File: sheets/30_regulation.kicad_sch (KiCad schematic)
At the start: 0 parts

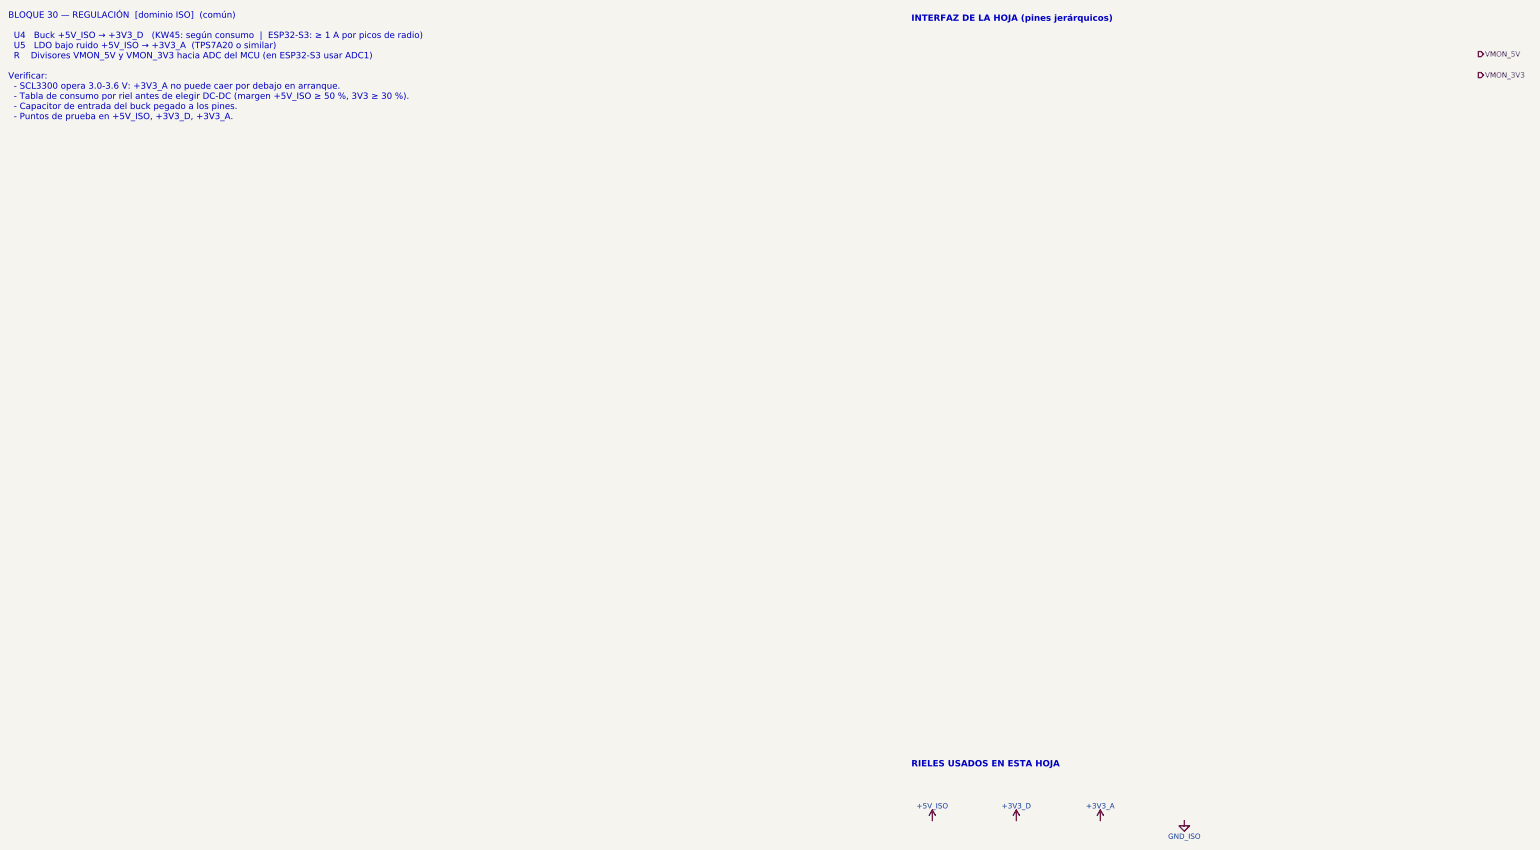
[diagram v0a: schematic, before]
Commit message: 30_regulation: buck TPS62A02-Q1 (+3V3_D), LDO LP5907-Q1 (+3V3_A) y VMON
- U301 TPS62A02QDRLRQ1 (+5V_ISO -> +3V3_D, 2 A, 2.2 MHz, PSM):
  L301 XAL4020-102MEC 1 uH (Isat 8.7 A); FB R303 453k / R304 100k ->
  3.318 V, C_FF C303 10 pF (TI); C_IN 10 uF 0805 + 100 nF; C_OUT C304
  22 uF 0805 (presupuesto de 47 uF en +3V3_D con el módulo); EN con
  pull-up; PG con pull-up a +3V3_D y test point.
- U302 LP5907QMFX-3.3Q1 (+5V_ISO -> +3V3_A) detrás de la ferrita FB301,
  C_IN/C_OUT 1 uF, PWR_FLAG en la entrada.
- VMON_5V (100k/49.9k) y VMON_3V3 (100k/100k) con 100 nF hacia ADC1.
- Test points en +5V_ISO, +3V3_D, +3V3_A, GND_ISO y PG.
- Símbolos TPS62A02QDRLRQ1 y TPS7A1650QDGNRQ1 (easyeda2kicad) reescritos:
  tipos de pin según TI, fabricante y datasheet de TI, y huellas
  oficiales de KiCad (SOT-563 y HVSSOP-8 EP1.57x1.89 con vías), que se
  acercan más a los land patterns TI DRL0006A y DGN0008B/C que las de
  EasyEDA. Huellas EasyEDA con ruta 3D ${KIPRJMOD}.

ERC de la hoja: 0 violaciones (total del proyecto 160 -> 149).
sch_visual_qa: PASS.

Co-Authored-By: Claude Opus 5.5 <noreply@anthropic.com>
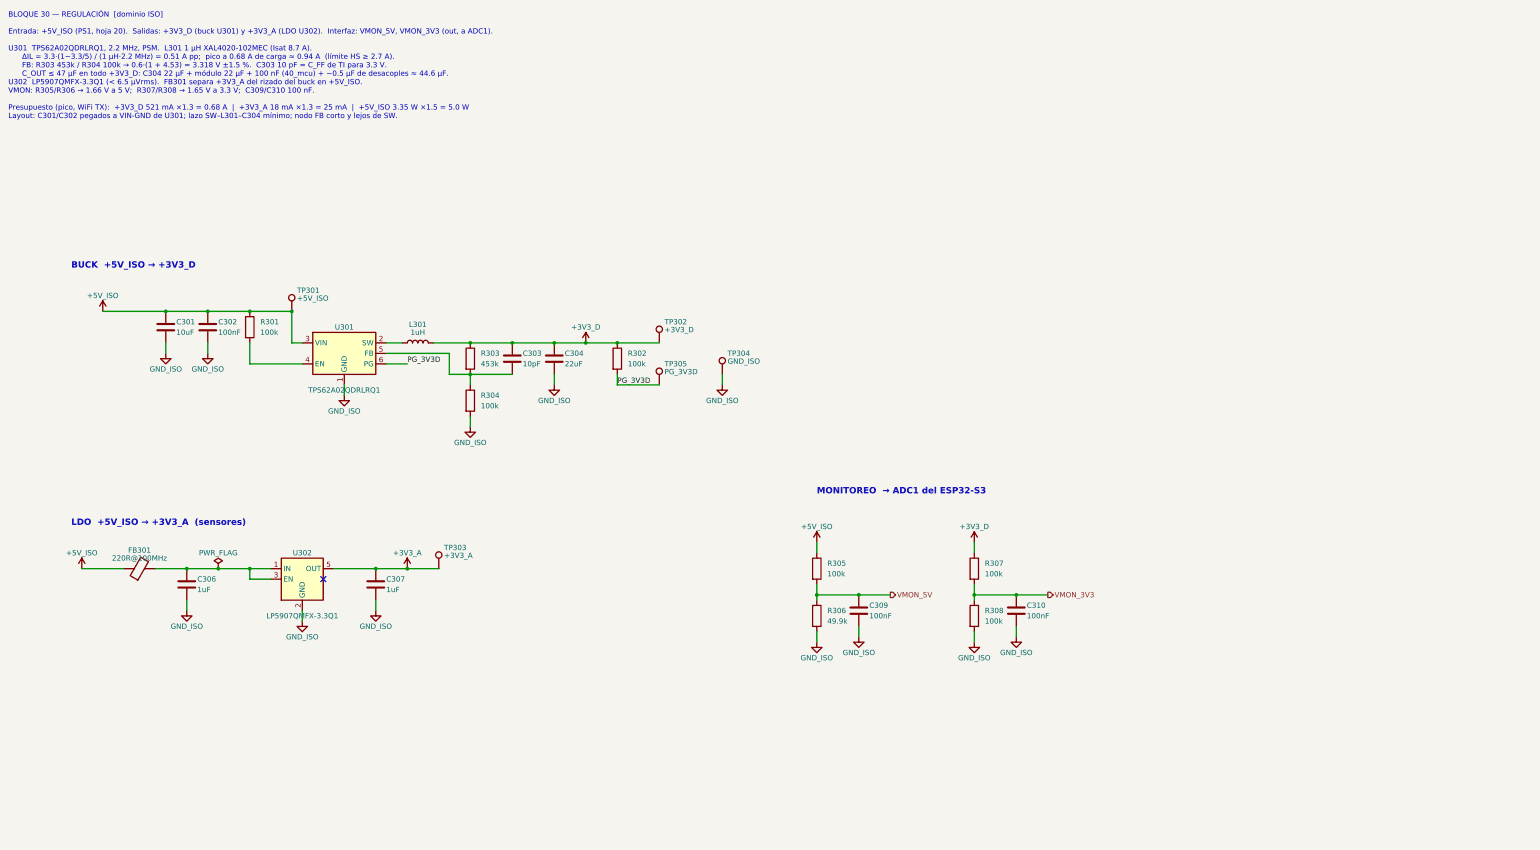
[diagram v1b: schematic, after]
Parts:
- added C301: 10uF, Capacitor_SMD:C_0805_2012Metric, symbol Device:C
- added C302, C309, C310: 100nF, Capacitor_SMD:C_0603_1608Metric, symbol Device:C
- added C303: 10pF, Capacitor_SMD:C_0603_1608Metric, symbol Device:C
- added C304: 22uF, Capacitor_SMD:C_0805_2012Metric, symbol Device:C
- added C306, C307: 1uF, Capacitor_SMD:C_0603_1608Metric, symbol Device:C
- added FB301: 220R@100MHz, Inductor_SMD:L_0603_1608Metric, symbol Device:FerriteBead
- added L301: 1uH, Inductor_SMD:L_Coilcraft_XAL4020-XXX, symbol Device:L
- added R301, R302, R304, R305, R307, R308: 100k, Resistor_SMD:R_0603_1608Metric, symbol Device:R
- added R303: 453k, Resistor_SMD:R_0603_1608Metric, symbol Device:R
- added R306: 49.9k, Resistor_SMD:R_0603_1608Metric, symbol Device:R
- added TP301: +5V_ISO, TestPoint:TestPoint_Pad_D1.5mm, symbol Connector:TestPoint
- added TP302: +3V3_D, TestPoint:TestPoint_Pad_D1.5mm, symbol Connector:TestPoint
- added TP303: +3V3_A, TestPoint:TestPoint_Pad_D1.5mm, symbol Connector:TestPoint
- added TP304: GND_ISO, TestPoint:TestPoint_Pad_D1.5mm, symbol Connector:TestPoint
- added TP305: PG_3V3D, TestPoint:TestPoint_Pad_D1.5mm, symbol Connector:TestPoint
- added U301: TPS62A02QDRLRQ1, Package_TO_SOT_SMD:SOT-563, symbol easyeda2kicad:TPS62A02QDRLRQ1
- added U302: LP5907QMFX-3.3Q1, Package_TO_SOT_SMD:SOT-23-5, symbol Regulator_Linear:LP5907MFX-3.3
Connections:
- net +3V3_A: now also C307.1, TP303.1, U302.5 (OUT)
- net +3V3_D: now also C303.1, C304.1, L301.2, R302.1, R303.1, R307.1, TP302.1
- net +5V_ISO: now also C301.1, C302.1, FB301.1, R301.1, R305.1, TP301.1, U301.3 (VIN)
- net GND_ISO: now also C301.2, C302.2, C304.2, C306.2, C307.2, C309.2, C310.2, R304.2, R306.2, R308.2, TP304.1, U301.1 (GND), U302.2 (GND)
- net VMON_3V3: now also C310.1, R307.2, R308.1
- net VMON_5V: now also C309.1, R305.2, R306.1
- new net: C303.2, R303.2, R304.1, U301.5 (FB)
- new net: C306.1, FB301.2, U302.1 (IN), U302.3 (EN)
- new net: L301.1, U301.2 (SW)
- new net: R301.2, U301.4 (EN)
- new net PG_3V3D: R302.2, TP305.1, U301.6 (PG)
- no-connect marks 0 -> 1
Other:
- note added: "BLOQUE 30 — REGULACIÓN [dominio ISO] Entrada: +5V_ISO (PS1, hoja 20). Salidas: +3V3_D (buck U301) y +3V3_A (LDO U302). Interfaz: VMON_5V, VMON_3V3 (out, a ADC1). U301 TPS62A02QDRLRQ1, 2.2 MHz, PSM. L301 1 µH XAL4020-102MEC (Isat 8.7 A). ΔIL = 3.3·(1−3.3/5) / (1 µH·2.2 MHz) = 0.51 A pp; pico a 0.68 A de carga ≈ 0.94 A (límite HS ≥ 2.7 A). FB: R303 453k / R304 100k → 0.6·(1 + 4.53) = 3.318 V ±1.5 %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"
- note added: "BUCK +5V_ISO → +3V3_D"
- note added: "LDO +5V_ISO → +3V3_A (sensores)"
- note added: "MONITOREO → ADC1 del ESP32-S3"
- note removed: "BLOQUE 30 — REGULACIÓN [dominio ISO] (común) U4 Buck +5V_ISO → +3V3_D (KW45: según consumo | ESP32-S3: ≥ 1 A por picos de radio) U5 LDO bajo ruido +5V_ISO → +3V3_A (TPS7A20 o similar) R Divisores VMON_5V y VMON_3V3 hacia ADC del MCU (en ESP32-S3 usar ADC1) Verificar: - SCL3300 opera 3.0-3.6 V: +3V3_A no puede caer por debajo en arranque. - Tabla de consumo por riel antes de elegir DC-DC (margen +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"
- note removed: "INTERFAZ DE LA HOJA (pines jerárquicos)"
- note removed: "RIELES USADOS EN ESTA HOJA"

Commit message: 20_isolation: PS201 EC4AW8-48S05, LDO +5V_VEH, ISO7763-Q1; PWR_FLT_N; L301 HandSolder
- Hoja 20 completa: PS201 Cincon EC4AW8-48S05 (sin Remote On/Off) con
  C201/C202/C203; U201 TPS7A1650-Q1 (+VPROT -> +5V_VEH; DELAY, PG y FB/NC
  abiertos según TI SBVS188E tabla 5-1); U202 ISO7763FQDWRQ1 con pull-downs
  R201-R204; notas de distancias de la barrera 1.
- Símbolo INCLI-VA:EC4AW8-48S05 creado desde la tabla de pines del datasheet
  Cincon V10 (excepción autorizada); huella oficial TRACO THD 15WIN verificada.
- Renombre PWR_FLT -> PWR_FLT_N en la raíz, 20 y 40_mcu.
- Huella INCLI-VA:L_Coilcraft_XAL4020_HandSolder (Coilcraft Doc 806-4,
  rev. 02/25/26) asignada a L301.
- Datasheets de EC4AW8 y XAL4020 en docs/datasheets.
- ERC: 0 en 20 y 30 (129 en el proyecto); sch_visual_qa PASS en 20.

Co-Authored-By: Claude Opus 5.5 <noreply@anthropic.com>
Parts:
- L301: footprint Inductor_SMD:L_Coilcraft_XAL4020-XXX -> INCLI-VA:L_Coilcraft_XAL4020_HandSolder; Notes 1.0 uH +-20 %, Isat 8.7 A, DCR 14.6 mohm máx, AEC-Q200. Isat > límite de corriente de U301 (3.3 A máx) para soportar el corto. TI admite 0.3-1.2 uH efectivos. Huella oficial KiCad. -> 1.0 uH +-20 %, Isat 8.7 A, DCR 14.6 mohm máx, AEC-Q200. Isat > límite de corriente de U301 (3.3 A máx) para soportar el corto. TI admite 0.3-1.2 uH efectivos. Huella INCLI-VA:L_Coilcraft_XAL4020_HandSolder: land pattern de Coilcraft Doc 806-4 (rev. 02/25/26, 0.98 x 3.4 mm, centros 2.37 mm) con pads extendidos 1 mm fuera del cuerpo para soldar a mano. En producción volver a Inductor_SMD:L_Coilcraft_XAL4020-XXX.
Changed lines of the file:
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@@
 			)
 		)
-		(property "Footprint" "Inductor_SMD:L_Coilcraft_XAL4020-XXX"
+		(property "Footprint" "INCLI-VA:L_Coilcraft_XAL4020_HandSolder"
 			(at 119.38 100.33 0)
 			(show_name no)
@@
 			)
 		)
-		(property "Notes" "1.0 uH +-20 %, Isat 8.7 A, DCR 14.6 mohm máx, AEC-Q200. Isat > límite de corriente de U301 (3.3 A máx) para soportar el corto. TI admite 0.3-1.2 uH efectivos. Huella oficial KiCad."
+		(property "Notes" "1.0 uH +-20 %, Isat 8.7 A, DCR 14.6 mohm máx, AEC-Q200. Isat > límite de corriente de U301 (3.3 A máx) para soportar el corto. TI admite 0.3-1.2 uH efectivos. Huella INCLI-VA:L_Coilcraft_XAL4020_HandSolder: land pattern de Coilcraft Doc 806-4 (rev. 02/25/26, 0.98 x 3.4 mm, centros 2.37 mm) con pads extendidos 1 mm fuera del cuerpo para soldar a mano. En producción volver a Inductor_SMD:L_Coilcraft_XAL4020-XXX."
 			(at 119.38 100.33 0)
 			(show_name no)

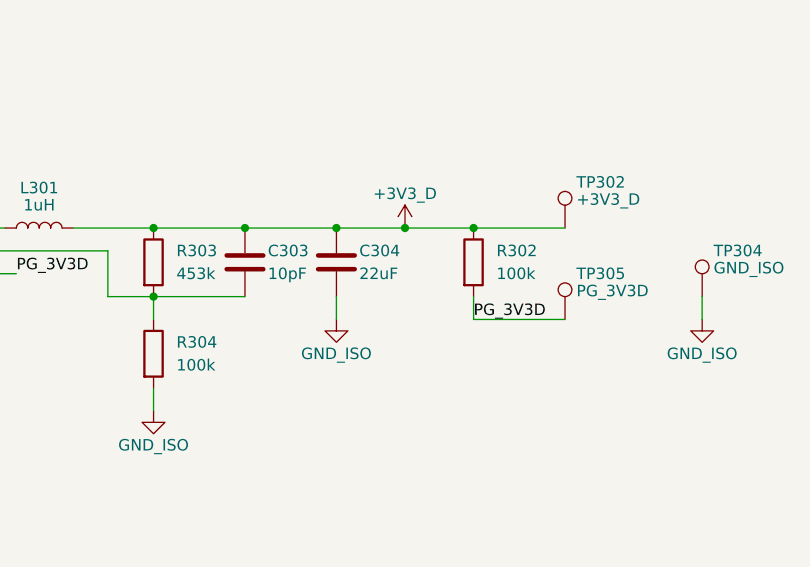
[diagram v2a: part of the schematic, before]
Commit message: [Claude Code] 40_mcu_esp32s3: ESP32-S3-WROOM-1-N8R2, USB-C nativo, UART0 (fase 4)
- U401 ESP32-S3-WROOM-1-N8R2 (símbolo y huella oficiales). Asignación de
  pines aprobada: VMON en ADC1, señales críticas (DO_EN, DIAG, PWR_FLT_N,
  CAN, IMU_INT) en pines sin glitch de encendido, SPI en IO MUX de FSPI,
  strapping/USB/UART0 reservados. Tabla y criterios en la hoja.
- Desacople 22 uF + 100 nF (presupuesto de 47 uF de +3V3_D).
- EN: 10k + 1 uF (Espressif) sobre MCU_RST_N; botones RESET y BOOT.
- USB-C GCT USB4105-GF-A + USBLC6-2SC6 en IO19/20; CC 5.1k; opción de
  banco DNP VBUS -> D401 -> JP401 -> +5V_ISO (~4.6 V, CAN no garantizado).
- Header UART0 (IO43/44), test points de EN, BOOT, VBUS, CAN_TX y CAN_RX.
- Nota de layout de la antena (borde, keepout, orientación respecto al chasis).
- 30_regulation: PWR_FLAG en +3V3_D (la red sale de L301, pasivo).
- ERC 0 en 40 y 30 (100 en el proyecto); sch_visual_qa PASS en ambas.
- docs/PENDIENTES.md: requisitos para 50 (pull-ups de CS a +3V3_A) y 80
  (pull-down en WD_EN), MPN a verificar de la hoja 40.

Co-Authored-By: Claude Opus 5.5 <noreply@anthropic.com>
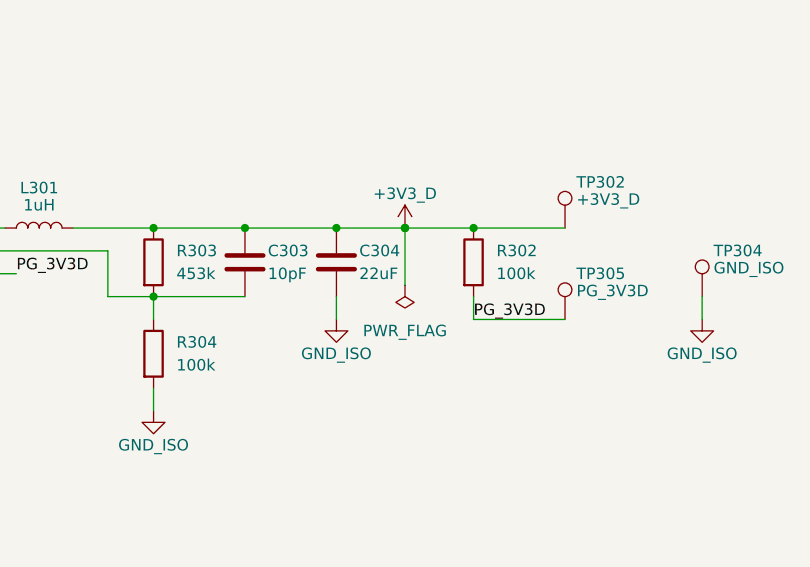
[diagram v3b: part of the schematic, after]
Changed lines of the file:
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@@
 		)
+	)
+	(symbol
+		(lib_id "power:PWR_FLAG")
+		(at 160.02 106.68 180)
+		(unit 1)
+		(body_style 1)
+		(exclude_from_sim no)
+		(in_bom no)
+		(on_board yes)
+		(in_pos_files no)
+		(dnp no)
+		(property "Reference" "#FLG302"
+			(at 160.02 102.87 0)
+			(show_name no)
+			(do_not_autoplace no)
+			(hide yes)
+			(effects
+				(font
+					(size 1.27 1.27)
+				)
+			)
+		)
+		(property "Value" "PWR_FLAG"
+			(at 160.02 111.76 0)
+			(show_name no)
+			(do_not_autoplace no)
+			(effects
+				(font
+					(size 1.27 1.27)
+				)
+			)
+		)
+		(property "Footprint" ""
+			(at 160.02 106.68 0)
+			(show_name no)
+			(do_not_autoplace no)
+			(hide yes)
+			(effects
+				(font
+					(size 1.27 1.27)
+				)
+			)
+		)
+		(property "Datasheet" ""
+			(at 160.02 106.68 0)
+			(show_name no)
+			(do_not_autoplace no)
+			(hide yes)
+			(effects
+				(font
+					(size 1.27 1.27)
+				)
+			)
+		)
+		(property "Description" ""
+			(at 160.02 106.68 0)
+			(show_name no)
+			(do_not_autoplace no)
+			(hide yes)
+			(effects
+				(font
+					(size 1.27 1.27)
+				)
+			)
+		)
+		(pin "1"
+		)
+		(instances
+			(project "INCLI-VA"
+				(path "/7fd92c2b-4254-4d73-93ba-bfde861bede3/e820859b-353c-4670-907b-04aca6cb5816"
+					(reference "#FLG302")
+					(unit 1)
+				)
+			)
+		)
+	)
+	(wire
+		(pts
+			(xy 160.02 100.33) (xy 160.02 106.68)
+		)
+		(stroke
+			(width 0)
+			(type default)
+		)
+	)
+	(junction
+		(at 160.02 100.33)
+		(diameter 0)
+		(color 0 0 0 0)
 	)
 	(no_connect
